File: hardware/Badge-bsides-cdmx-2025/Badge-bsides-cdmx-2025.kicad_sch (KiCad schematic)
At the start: 25 parts, among them J1 SWDIO, J2 Conn_01x02_Pin, J4 Conn_01x02_Pin, J5 Battery, P6 USB_C_Plug_USB2.0, Q3 DMG3415U-7, SW11 ON, U1 PY32F030F28U6TR, U6 AP2112K-3.3

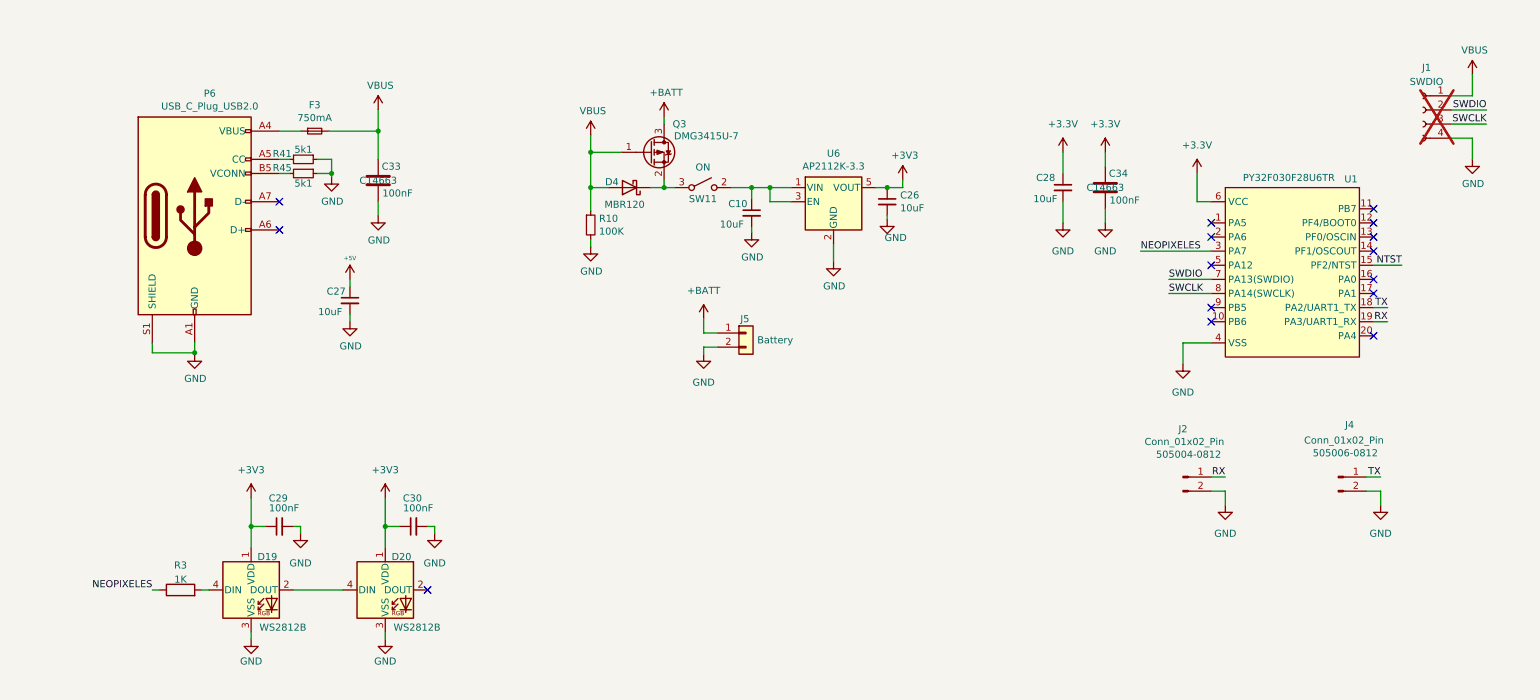
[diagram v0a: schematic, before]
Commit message: FIx(Hw): Fixed_Bom_and_footprints
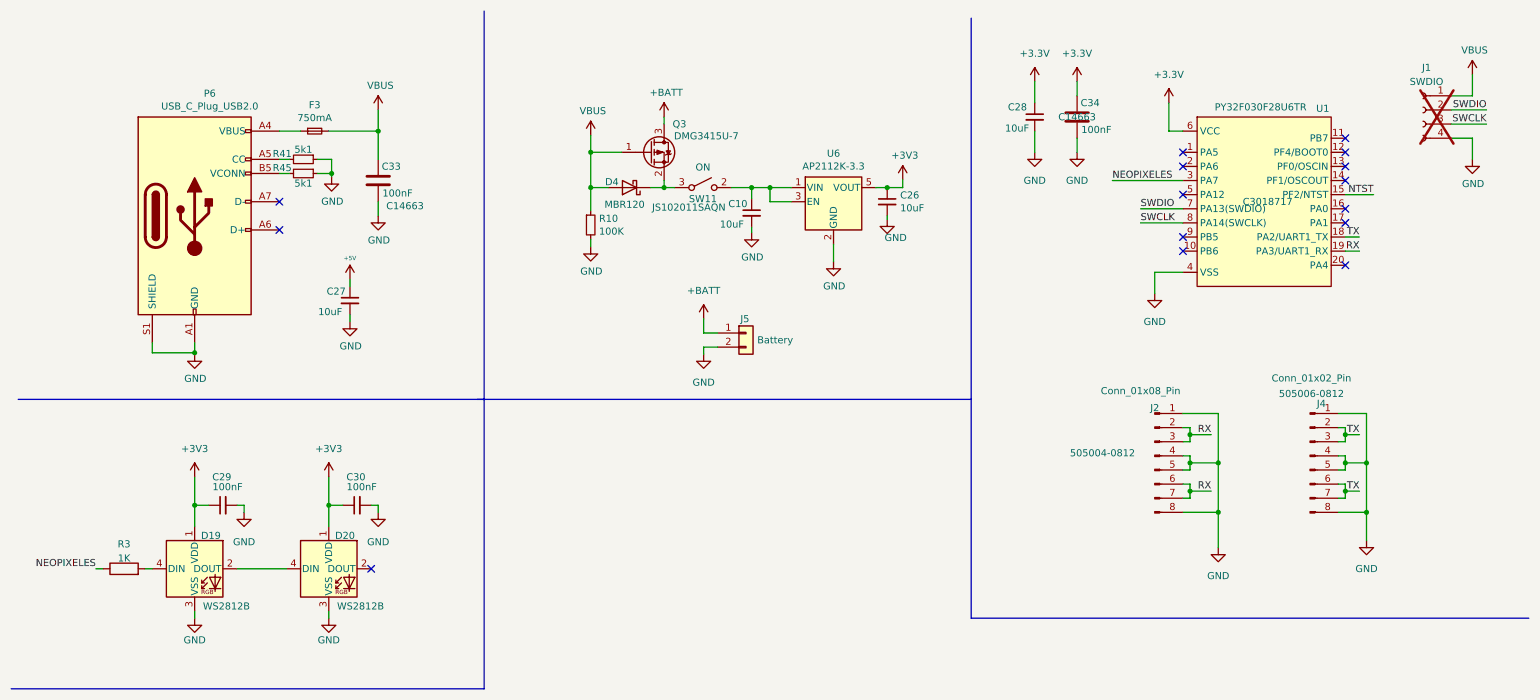
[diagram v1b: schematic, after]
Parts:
- J2: value Conn_01x02_Pin -> Conn_01x08_Pin; symbol Connector:Conn_01x02_Pin -> Connector:Conn_01x08_Pin; LCSC# 505004-0812 -> (none); Manufacturer_Part_Number (none) -> 505004-0812
- J4: symbol Connector:Conn_01x02_Pin -> Connector:Conn_01x08_Pin; LCSC# 505006-0812 -> (none); Manufacturer_Part_Number (none) -> 505006-0812
- J5: footprint (none) -> Footprints:BAT-TH_BH-AAA-A1AJ024; LCSC# C3029440 -> C5290193
- P6: #LCSC C2760486 -> (none)
- R41, R45: #LCSC C191782 -> (none)
- SW11: footprint footprints:JS102011SAQN -> Footprints:JS102011SAQN; Manufacturer_Part_Number (none) -> JS102011SAQN
- U1: LCSC# (none) -> C3018717
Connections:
- net GND: now also J2.1 (Pin_1), J2.4 (Pin_4), J2.5 (Pin_5), J2.8 (Pin_8), J4.1 (Pin_1), J4.4 (Pin_4), J4.5 (Pin_5), J4.8 (Pin_8); no longer J2.2 (Pin_2), J4.2 (Pin_2)
- net RX: now also J2.2 (Pin_2), J2.3 (Pin_3), J2.6 (Pin_6), J2.7 (Pin_7); no longer J2.1 (Pin_1)
- net TX: now also J4.2 (Pin_2), J4.3 (Pin_3), J4.6 (Pin_6), J4.7 (Pin_7); no longer J4.1 (Pin_1)
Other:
- moved on the sheet: C28, C29, C30, C34, D19, D20, R3, U1

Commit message: feat: add button RST and shitty connector
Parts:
- added C6: 100nF, Capacitor_SMD:C_0603_1608Metric, symbol Device:C_Small
- added J3: ADDON, Connector_PinSocket_2.54mm:PinSocket_2x03_P2.54mm_Vertical_SMD, symbol Connector_Generic:Conn_02x03_Odd_Even
- added R4: 10k, Resistor_SMD:R_0603_1608Metric, symbol Device:R_Small
- added SW2: RESET, Button_Switch_SMD:SW_SPST_TL3342, symbol Switch:SW_Push
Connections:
- net +3V3: now also J3.1 (Pin_1), R4.2
- net GND: now also C6.2, J3.2 (Pin_2), SW2.1
- net NTST: now also C6.1, R4.1, SW2.2
- new net GPIO1: J3.5 (Pin_5)
- new net GPIO2: J3.6 (Pin_6)
- new net SCL: J3.4 (Pin_4)
- new net SDA: J3.3 (Pin_3)
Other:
- note added: "SHITTY-ADDON"
- title: (none) -> Bsides cDMX 2025
